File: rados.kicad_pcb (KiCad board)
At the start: 2 copper layers, 83.5 x 106 mm, 156 parts, among them J1 HEADER, J10 STEPSTICK, J11 STEPSTICK, J12 STEPSTICK, J13 MICROSD_SLOT_TFP09-2-12B, J2 HEADER, J3 HEADER, J4 STEPSTICK, J5 STEPSTICK, J6 STEPSTICK, J7 HEADER, J8 HEADER, J9 HEADER, P1 CONN_01X02, P10 CONN_01X04, P11 CONN_01X04, P12 CONN_01X04, P13 EXT_SD, P14 LCD, P15 LIMIT_SWITCHES, P16 LIMIT_SWITCHES_V, P17 CONN_01X03, P18 CONN_01X03, P19 CONN_01X03, P2 CONN_01X02, P20 CONN_01X03, P21 THERMISTORS, P22 CONN_01X05, P23 CONN_01X02, P24 CONN_01X02, P3 CONN_01X02, P4 CONN_01X02, P5 HP_MOSFETS, P6 MP_MOSFETS, P7 CONN_02X04, P8 CONN_01X04, P9 CONN_01X04, Q1 2N7002P, Q10 2N7002P, Q11 2N7002P, Q12 BC846BPDW1, Q13 BC846BPDW1, Q14 SI2318CDS-T1-GE3, Q15 IRFB7545PbF, Q16 2N7002P, Q17 2N7002P, Q18 BC846BPDW1, Q19 BC846BPDW1, Q2 2N7002P, Q20 SI2318CDS-T1-GE3, Q21 IRFB7545PbF, Q3 2N7002P, Q4 BC846BPDW1, Q5 BC846BPDW1, Q6 BC846BPDW1, Q7 IRFB7545PbF, Q8 SI2318CDS-T1-GE3, Q9 IRFB7545PbF, SW1 RESET, U1 ST1S14PHR, U2 24LC256, U3 ESP-12E

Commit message: Fixed some TODO's
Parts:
- added C36: 10uF, capacitors:C_0805, F.Cu at (98.4, 51.2)
- added P25: CONN_01X03, headers:CON_HDR_1x3_2.54mm, F.Cu at (109.2, 27.9)
- moved Q10 5.21 mm to (95.0, 53.8)
- moved R6 4.50 mm to (99.0, 92.7)
- moved R16 3.60 mm to (98.6, 54.0), turned to 0 degrees
- moved R25 2.63 mm to (100.6, 78.0), turned to 0 degrees
- moved R17 2.00 mm to (100.6, 80.0), turned to 0 degrees
- moved R42 1.48 mm to (119.3, 122.7)
- moved Q16 1.24 mm to (106.2, 29.2)
- moved R24 0.43 mm to (106.4, 25.2)
- moved C33 0.15 mm to (111.8, 26.4)
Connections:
- SHIELD1 pad 1: Y-EN -> Net-(SHIELD1-Pad1)
- SHIELD1 pad 10: SD-CS -> Z-STEP
- SHIELD1 pad 15: MP-FET1 -> Y-EN
- SHIELD1 pad 22: LP-FET2 -> Net-(SHIELD1-Pad22)
- SHIELD1 pad 23: Net-(SHIELD1-Pad23) -> LP-FET2
- SHIELD1 pad 25: LP-FET1 -> Net-(SHIELD1-Pad25)
- SHIELD1 pad 4: HP-FET3 -> MP-FET1
- SHIELD1 pad 5: HP-FET2 -> LP-FET1
- SHIELD1 pad 6: HP-FET1 -> HP-FET3
- SHIELD1 pad 7: HB-FET -> HP-FET2
- SHIELD1 pad 8: Z-STEP -> HP-FET1
- SHIELD1 pad 9: ENC-SW -> HB-FET
- SHIELD1 pad SCL1: Net-(SHIELD1-PadSCL1) -> SD-CS
- SHIELD1 pad SDA1: Net-(SHIELD1-PadSDA1) -> ENC-SW
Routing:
- net SDA1: track 0.24 -> 49.2 mm
- net SCL1: track 0.00 -> 48.9 mm
- net RESET: track 77.6 -> 53.2 mm
- net SD-CS: track 80.7 -> 62.2 mm
- net Z-EN: track 39.6 -> 21.8 mm
- net MP-FET1: track 3.33 -> 20.8 mm, vias 0 -> 2
- net ENC-SW: track 49.6 -> 32.4 mm
- net X-EN: track 2.93 -> 17.3 mm
- net GND: track 81.8 -> 90.6 mm, vias 58 -> 63
- net Y-EN: track 22.8 -> 31.5 mm
- net ESP-RX: track 32.4 -> 26.1 mm
- net HB-FET: track 21.0 -> 15.6 mm
- net Z-STEP: track 11.3 -> 6.27 mm
- net HP-FET3: track 15.4 -> 20.2 mm
- net ESP-TX: track 29.1 -> 24.5 mm
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
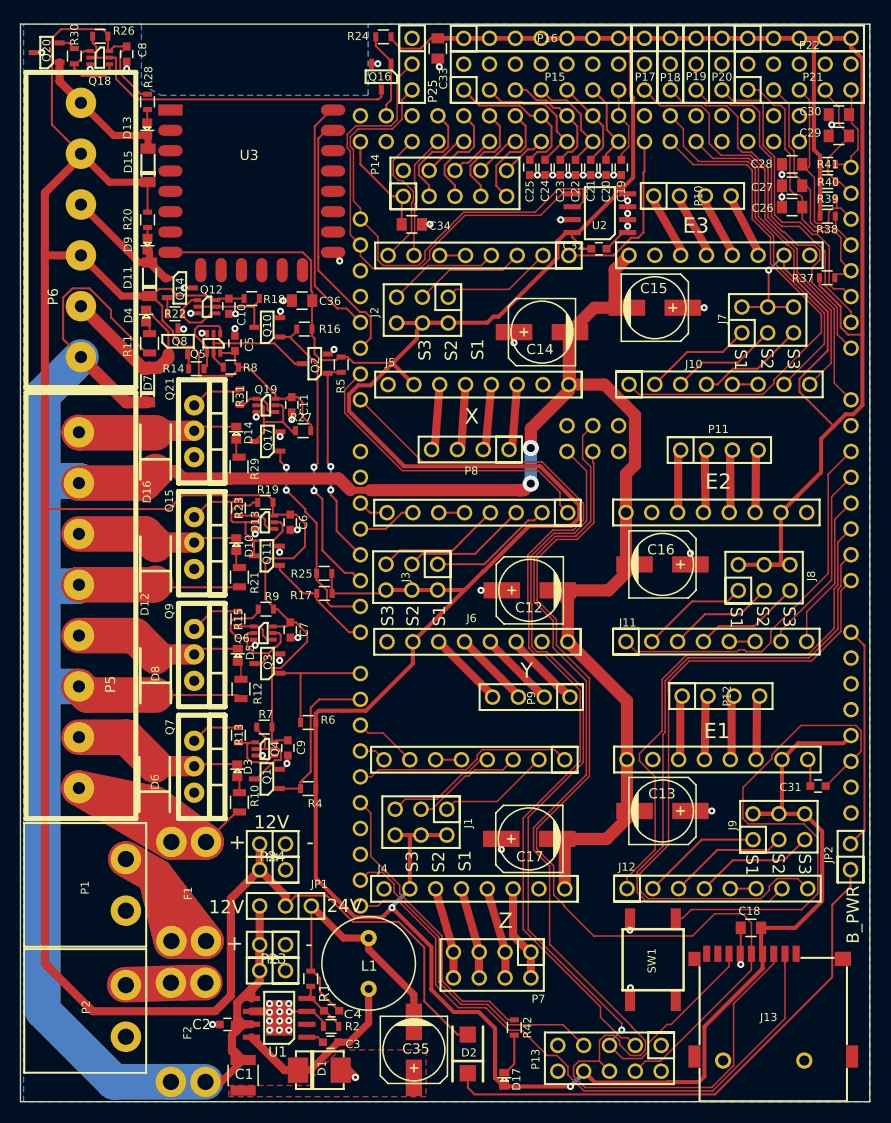
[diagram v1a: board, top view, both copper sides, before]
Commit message: Added minimal arduino mega support
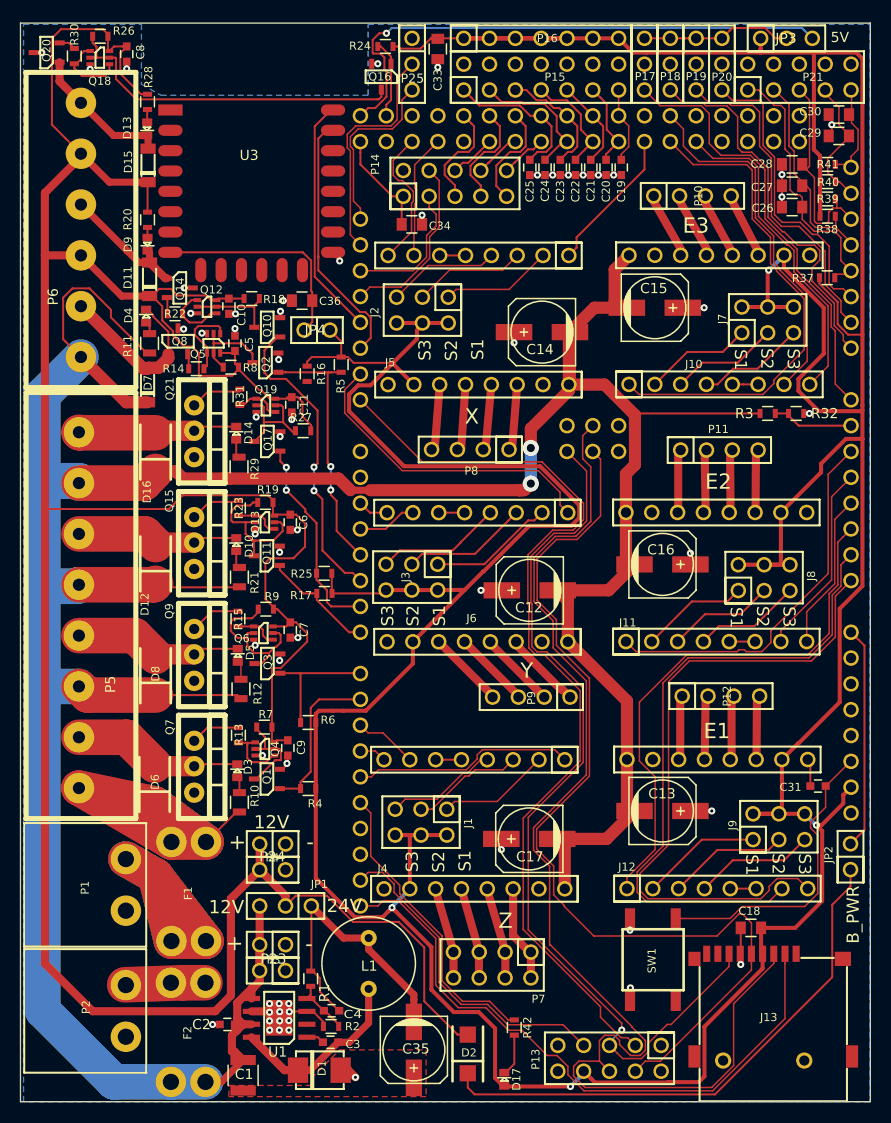
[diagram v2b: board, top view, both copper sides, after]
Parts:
- removed C32: 100nF, capacitors:C_0603
- removed P22: CONN_01X05, headers:CON_HDR_1x5_2.54mm
- removed U2: 24LC256, soic:SOIC8
- added JP3: AUX_VSEL, headers:CON_HDR_1x3_2.54mm, F.Cu at (146.1, 25.4)
- added JP4: Jumper_NC_Small, headers:CON_HDR_1x2_2.54mm, F.Cu at (99.9, 54.1)
- added R3: 22K, resistors:R_0603, F.Cu at (144.2, 62.3)
- added R32: 2K, resistors:R_0603, F.Cu at (147.0, 62.3)
- P25: value CONN_01X03 -> I2C
- moved Q2 4.85 mm to (94.8, 57.3)
- moved R16 4.41 mm to (98.9, 58.4), turned to 90 degrees
- moved R24 0.97 mm to (106.6, 26.2)
- moved C33 0.05 mm to (111.8, 26.4)
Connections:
- C36 pad 1: +3V3 -> Net-(C36-Pad1)
- P17 pad 1: +3V3 -> Net-(JP3-Pad2)
- P18 pad 1: +3V3 -> Net-(JP3-Pad2)
- P19 pad 1: +3V3 -> Net-(JP3-Pad2)
- P20 pad 1: +3V3 -> Net-(JP3-Pad2)
- SHIELD1 pad 18: Net-(SHIELD1-Pad18) -> ENC-B
- SHIELD1 pad 19: Net-(SHIELD1-Pad19) -> ENC-A
- SHIELD1 pad 27: ENC-A -> Net-(SHIELD1-Pad27)
- SHIELD1 pad 28: ENC-B -> Net-(SHIELD1-Pad28)
- SHIELD1 pad 3V3: +3V3 -> Net-(SHIELD1-Pad3V3)
- SHIELD1 pad AD6: Net-(SHIELD1-PadAD6) -> MEASURE-VSUPPLY
- SHIELD1 pad IORF: Net-(SHIELD1-PadIORF) -> +3V3
- U3 pad 8: +3V3 -> Net-(C36-Pad1)
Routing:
- net +3V3: track 533.8 -> 474.4 mm, vias 3 -> 4
- net +5V: track 10.7 -> 64.7 mm, vias 0 -> 1
- net SCL1: track 48.9 -> 17.6 mm
- net SDA1: track 49.2 -> 23.2 mm
- net RESET: track 53.2 -> 29.9 mm
- net Net-(C36-Pad1): track 0.00 -> 21.4 mm
- net Net-(JP3-Pad2): track 0.00 -> 14.9 mm
- net ENC-B: track 4.58 -> 17.8 mm
- net Vsupply: track 337.3 -> 349.7 mm
- net MEASURE-VSUPPLY: track 0.00 -> 8.06 mm
- net GND: track 90.6 -> 83.0 mm, vias 63 -> 60
- net MP-FET1: track 20.8 -> 26.0 mm
- net Net-(Q2-Pad3): track 13.2 -> 8.82 mm
- net X-EN: track 17.3 -> 14.3 mm
- net ENC-A: track 11.4 -> 13.7 mm
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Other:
- board size 83.5 x 106 mm -> 83.6 x 106.1 mm
- board text added: "5V"

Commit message: Added some names/logo's on silkscreen
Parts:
- added G***: LOGO, logos:OSHW-LOGO, B.Cu at (84.0, 55.1)
- added svg2mod: G***, logos:firemc-logo, F.Cu at (124.4, 43.5)
- added svg2mod: G***, logos:firemc-logo, B.Cu at (81.3, 37.5)
- added svg2mod: G***, logos:OtherUseLogo_medium, B.Cu at (91.9, 32.4)
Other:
- board text added: "Designed by"
- board text added: "open source hardware"

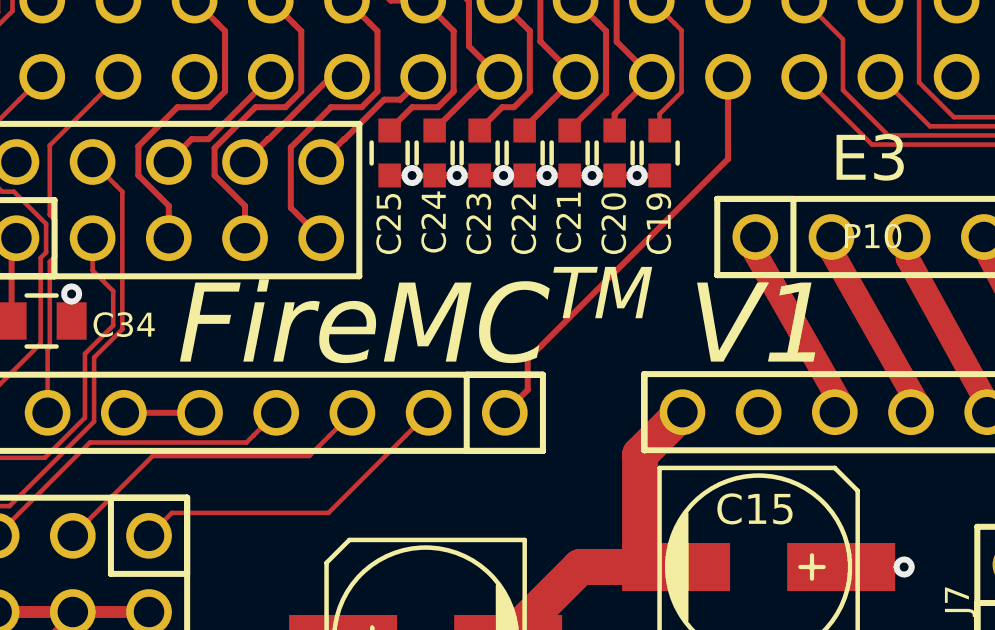
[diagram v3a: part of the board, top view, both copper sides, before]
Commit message: Added component specifications
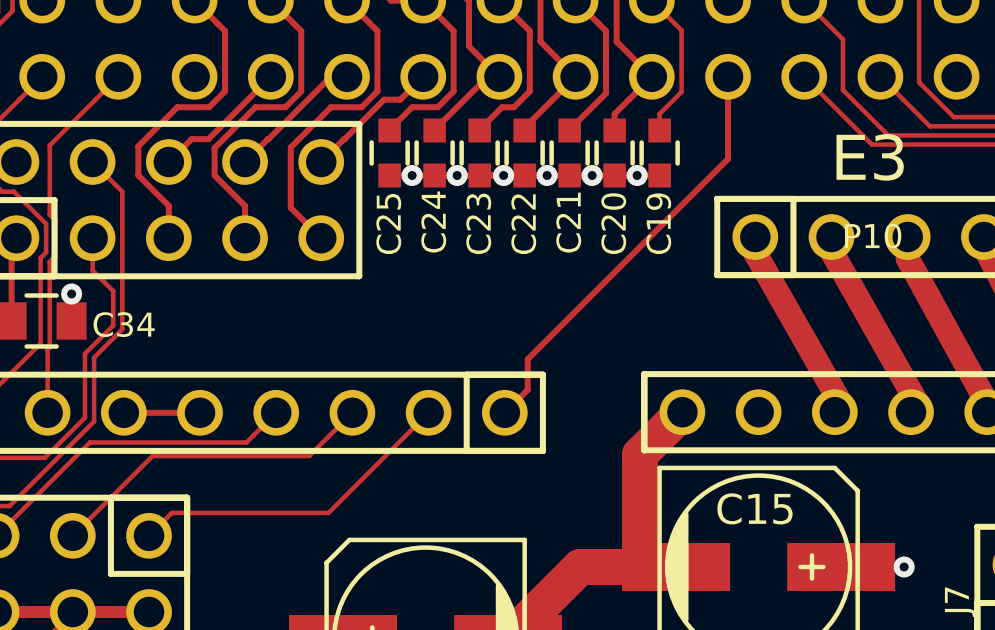
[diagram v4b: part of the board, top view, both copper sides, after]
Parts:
- removed G***: LOGO, logos:OSHW-LOGO
- removed svg2mod (x2): G***, logos:firemc-logo
- removed svg2mod: G***, logos:OtherUseLogo_medium
- D17: value Red -> Blue
- L1: value 18uF -> 18uH
- R13, R14, R15, R22, R23, R30, R31: value 5R -> 22R
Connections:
- Q12 pad 3: GND -> (no net)
- Q12 pad 4: Net-(Q12-Pad1) -> (no net)
- Q12 pad 5: Net-(Q10-Pad3) -> (no net)
- Q13 pad 3: GND -> (no net)
- Q13 pad 4: Net-(Q13-Pad1) -> (no net)
- Q13 pad 5: Net-(Q11-Pad3) -> (no net)
- Q13 pad 6: +12V -> GND
- Q18 pad 3: GND -> (no net)
- Q18 pad 4: Net-(Q18-Pad1) -> (no net)
- Q18 pad 5: Net-(Q16-Pad3) -> (no net)
- Q19 pad 3: GND -> (no net)
- Q19 pad 4: Net-(Q19-Pad1) -> (no net)
- Q19 pad 5: Net-(Q17-Pad3) -> (no net)
- Q4 pad 3: GND -> (no net)
- Q4 pad 4: Net-(Q4-Pad1) -> (no net)
- Q4 pad 5: Net-(Q1-Pad3) -> (no net)
- Q5 pad 3: GND -> (no net)
- Q5 pad 4: Net-(Q5-Pad1) -> (no net)
- Q5 pad 5: Net-(Q2-Pad3) -> (no net)
- Q6 pad 3: GND -> (no net)
- Q6 pad 4: Net-(Q6-Pad1) -> (no net)
- Q6 pad 5: Net-(Q3-Pad3) -> (no net)
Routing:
- net (no net): track 0.00 -> 3.99 mm, vias 0 -> 7
- net GND: track 83.0 -> 80.8 mm, vias 60 -> 53
- net +12V: track 301.2 -> 299.4 mm

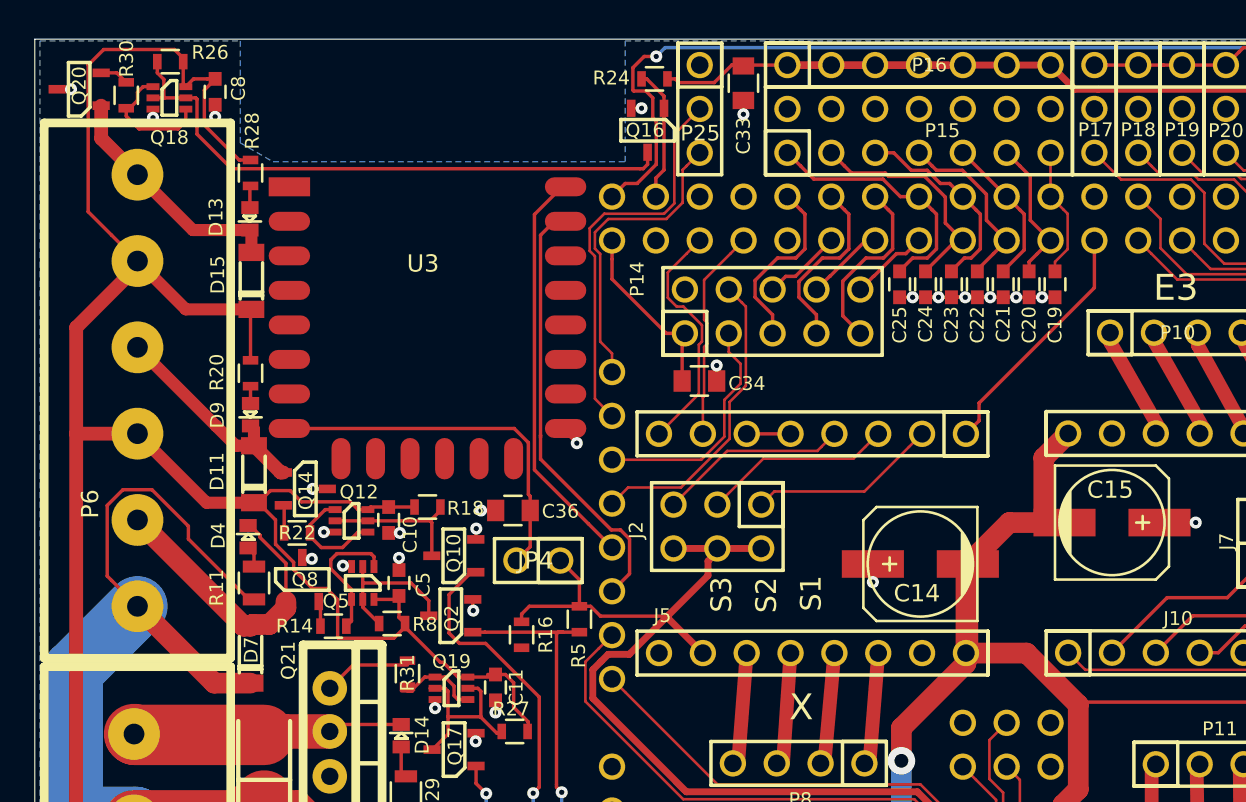
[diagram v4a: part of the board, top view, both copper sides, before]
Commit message: - Fix si2318 pinout - Fix slot problem introduced with attribute changes
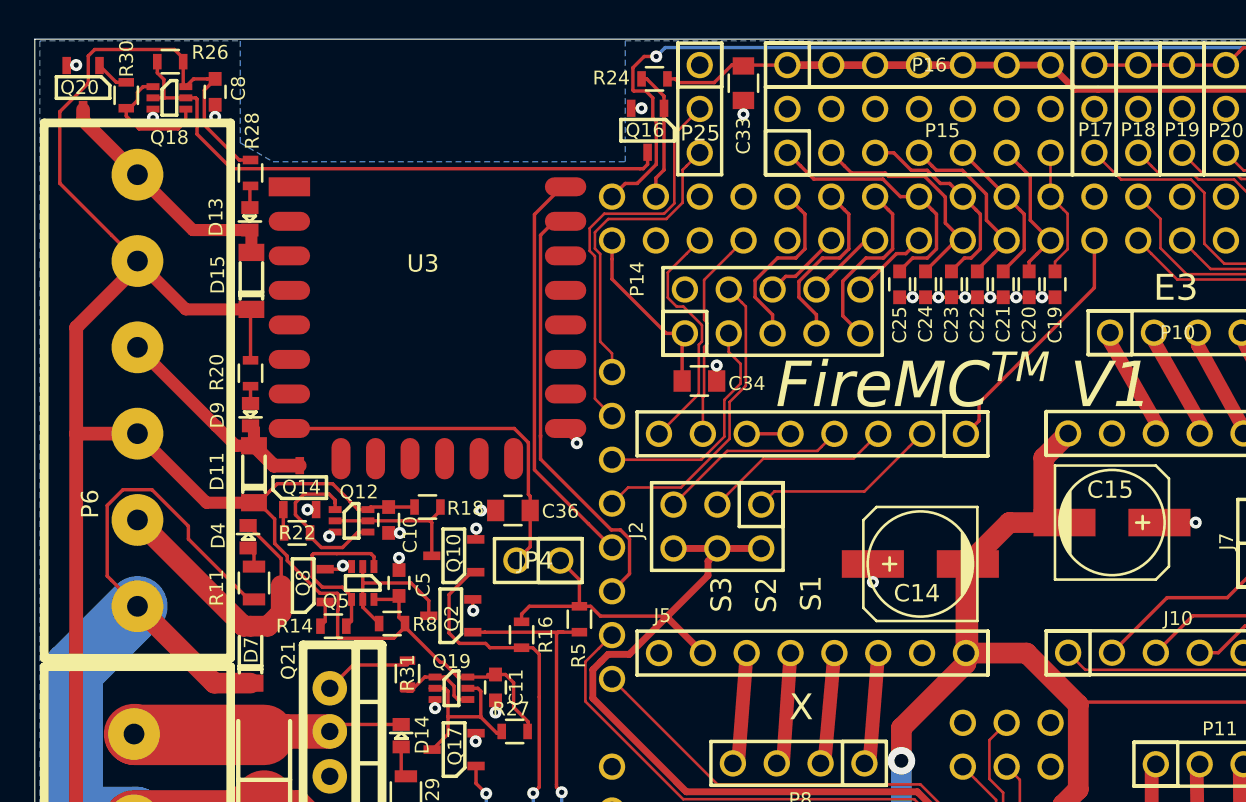
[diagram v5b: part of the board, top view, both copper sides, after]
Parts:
- added G***: LOGO, logos:OSHW-LOGO, B.Cu at (84.3, 55.0)
- added svg2mod: G***, logos:firemc-logo, F.Cu at (124.3, 43.6)
- added svg2mod: G***, logos:firemc-logo, B.Cu at (81.8, 35.8)
- added svg2mod: G***, logos:OtherUseLogo_medium, B.Cu at (92.1, 31.1)
- J1, J2, J3, J7, J8, J9: value HEADER -> CONN_02X03
- JP1: value VSEL -> CONN_01X03
- JP2: value BOARD_POWER -> CONN_01X02
- JP3: value AUX_VSEL -> CONN_01X03
- JP4: value Jumper_NC_Small -> CONN_01X02
- P13: value EXT_SD -> CONN_02x05
- P14: value LCD -> CONN_02x05
- P15: value LIMIT_SWITCHES -> CONN_02x07
- P16: value LIMIT_SWITCHES_V -> CONN_01X07
- P21: value THERMISTORS -> CONN_02x05
- P25: value I2C -> CONN_01X03
- P5: value HP_MOSFETS -> TERMINAL_BLOCK
- P6: value MP_MOSFETS -> TERMINAL_BLOCK
- SW1: value RESET -> BUTTON
- moved Q8 0.35 mm to (86.2, 55.5), turned to 180 degrees
- moved Q14 0.33 mm to (86.0, 49.9), turned to 90 degrees
- moved Q20 0.25 mm to (73.5, 26.7), turned to 270 degrees
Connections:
- Q12 pad 3: (no net) -> GND
- Q12 pad 4: (no net) -> Net-(Q12-Pad1)
- Q12 pad 5: (no net) -> Net-(Q10-Pad3)
- Q13 pad 3: (no net) -> GND
- Q13 pad 4: (no net) -> Net-(Q13-Pad1)
- Q13 pad 5: (no net) -> Net-(Q11-Pad3)
- Q13 pad 6: GND -> +12V
- Q14 pad 1: LP-OUT1 -> Net-(Q14-Pad1)
- Q14 pad 2: Net-(Q14-Pad2) -> GND
- Q14 pad 3: GND -> LP-OUT1
- Q18 pad 3: (no net) -> GND
- Q18 pad 4: (no net) -> Net-(Q18-Pad1)
- Q18 pad 5: (no net) -> Net-(Q16-Pad3)
- Q19 pad 3: (no net) -> GND
- Q19 pad 4: (no net) -> Net-(Q19-Pad1)
- Q19 pad 5: (no net) -> Net-(Q17-Pad3)
- Q20 pad 1: LP-OUT2 -> Net-(Q20-Pad1)
- Q20 pad 2: Net-(Q20-Pad2) -> GND
- Q20 pad 3: GND -> LP-OUT2
- Q4 pad 3: (no net) -> GND
- Q4 pad 4: (no net) -> Net-(Q4-Pad1)
- Q4 pad 5: (no net) -> Net-(Q1-Pad3)
- Q5 pad 3: (no net) -> GND
- Q5 pad 4: (no net) -> Net-(Q5-Pad1)
- Q5 pad 5: (no net) -> Net-(Q2-Pad3)
- Q6 pad 3: (no net) -> GND
- Q6 pad 4: (no net) -> Net-(Q6-Pad1)
- Q6 pad 5: (no net) -> Net-(Q3-Pad3)
- Q8 pad 1: MP-OUT1 -> Net-(Q8-Pad1)
- Q8 pad 2: Net-(Q8-Pad2) -> GND
- Q8 pad 3: GND -> MP-OUT1
- R14 pad 2: Net-(Q8-Pad2) -> Net-(Q8-Pad1)
- R22 pad 2: Net-(Q14-Pad2) -> Net-(Q14-Pad1)
- R30 pad 2: Net-(Q20-Pad2) -> Net-(Q20-Pad1)
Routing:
- net (no net): track 3.99 -> 0.00 mm, vias 7 -> 0
- net +12V: track 299.4 -> 303.3 mm
- net Net-(Q12-Pad1): track 6.48 -> 9.49 mm
- net Net-(Q5-Pad1): track 7.76 -> 10.1 mm
- net Net-(Q20-Pad1): track 0.00 -> 1.95 mm
- net GND: track 80.8 -> 82.8 mm, vias 53 -> 59
- net Net-(Q20-Pad2): track 1.68 -> 0.00 mm
- net Net-(Q14-Pad2): track 1.62 -> 0.00 mm
- net Net-(Q8-Pad1): track 0.00 -> 1.51 mm
- net Net-(Q8-Pad2): track 1.47 -> 0.00 mm
- net LP-FET1: track 30.3 -> 31.7 mm
- net Net-(Q14-Pad1): track 0.00 -> 1.37 mm
- net LP-OUT1: track 12.7 -> 13.5 mm
